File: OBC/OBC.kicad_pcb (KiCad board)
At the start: 4 copper layers, 90.3 x 95.8 mm, 53 parts

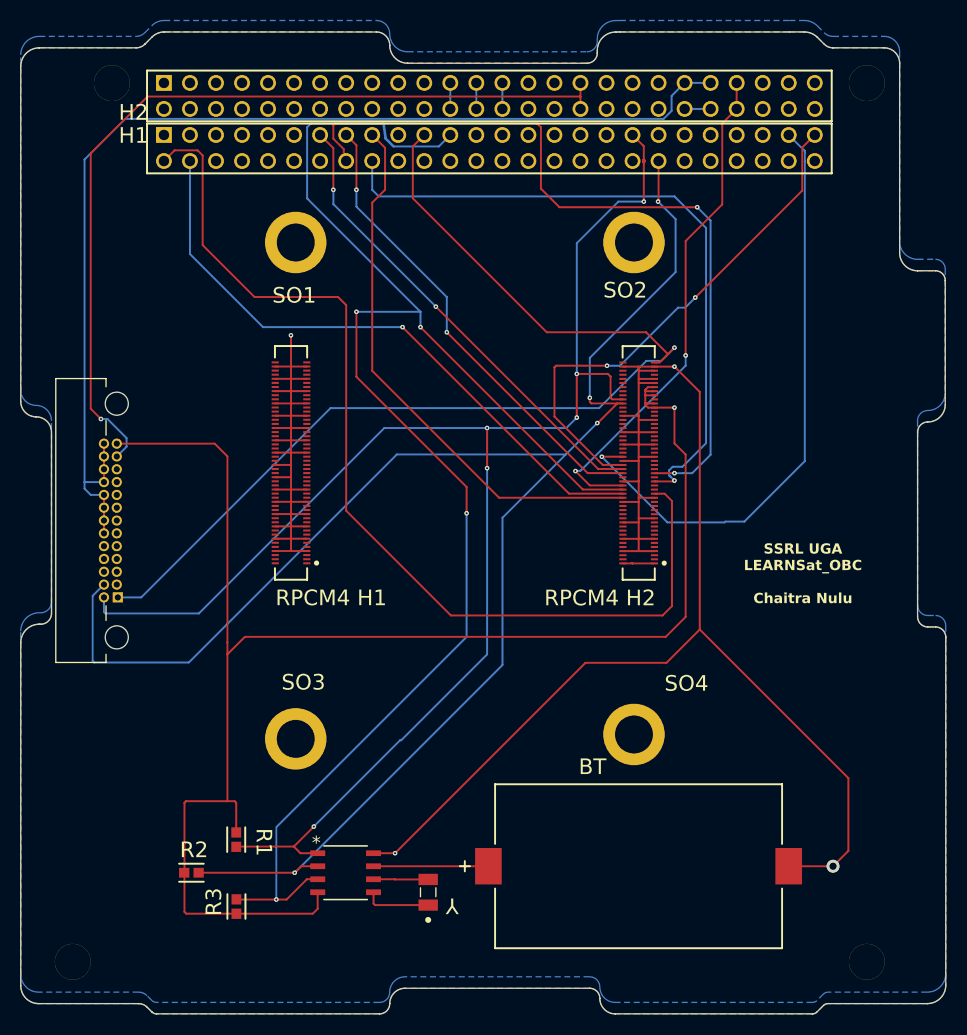
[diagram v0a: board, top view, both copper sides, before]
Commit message: OBC changes 9/23 Simon Ionashku
Fixed Positioning of S03 to be exactly 48.000 mm apart for the CM4 module mounting holes
Merged co-linear tracks
Deleted redundant graphics (24 zero-size segments)
Added Name to board
Fixed 8 same layer corners
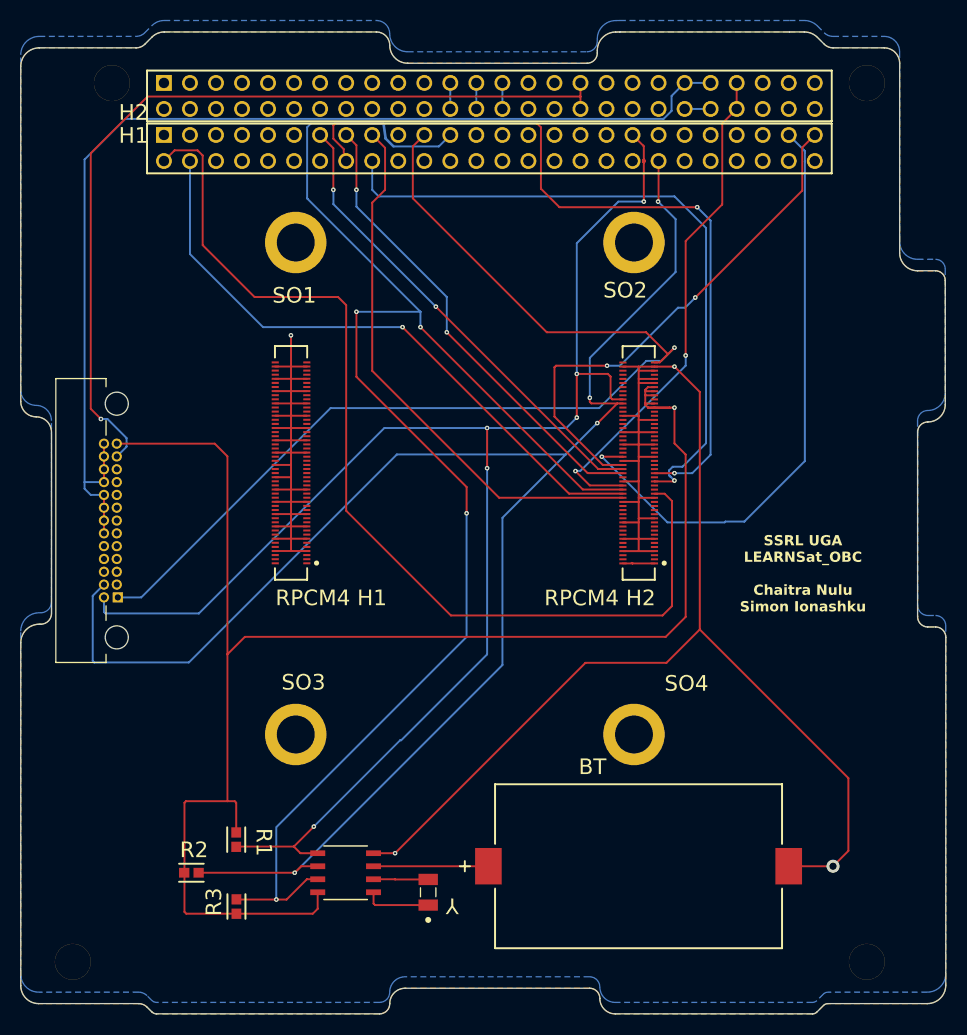
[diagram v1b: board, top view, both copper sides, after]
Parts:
- moved ? 0.43 mm to (130.2, 125.6)
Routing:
- net 5V_Primary: track 156.6 -> 158.5 mm
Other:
- board text added: "SSRL UGA LEARNSat_OBC Chaitra Nulu Simon Ionashku"
- board text removed: "*"
- board text removed: "SSRL UGA LEARNSat_OBC Chaitra Nulu"

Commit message: OBC changes 9/30 Simon Ionashku
deleted tiny hidden tracks that were hiding under other traces
Fixed clearance violations on the RPCM4 header
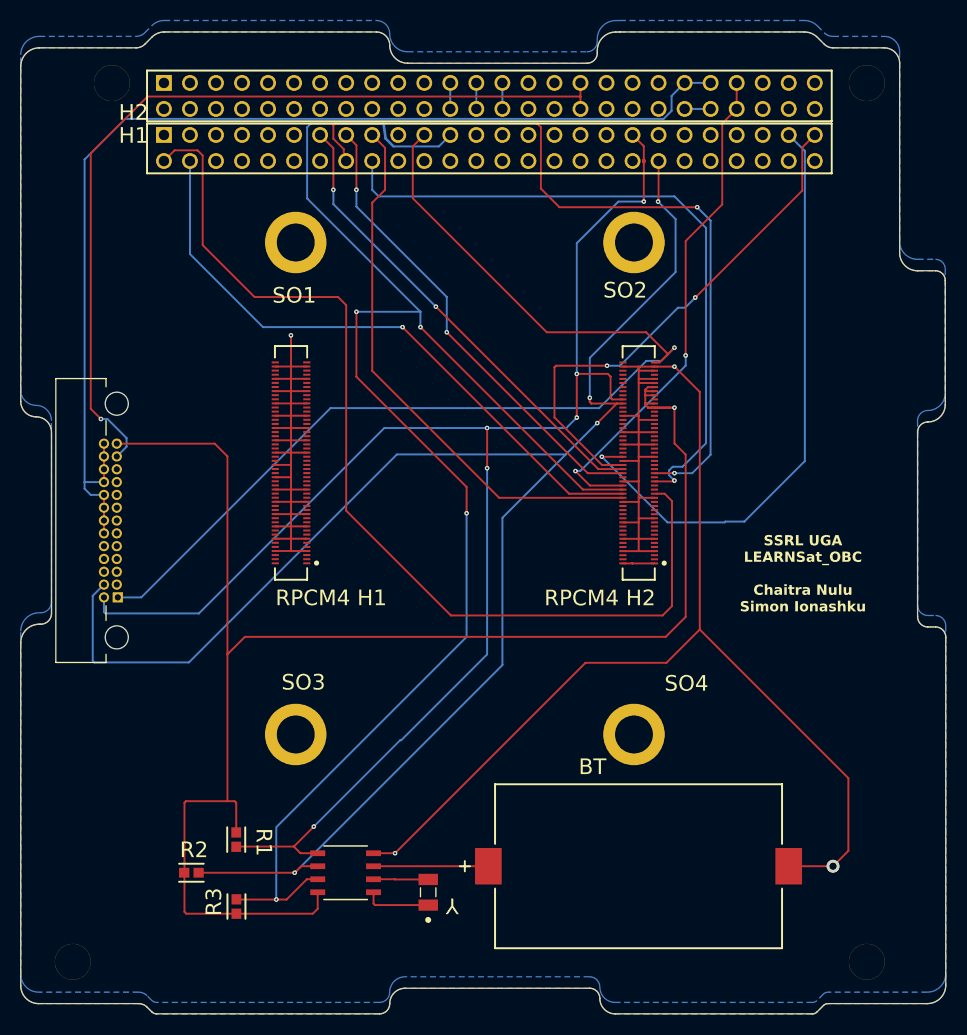
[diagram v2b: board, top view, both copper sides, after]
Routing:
- net SCL: track 164.3 -> 164.9 mm
